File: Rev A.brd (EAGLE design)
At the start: 160 x 100 mm, 21 parts

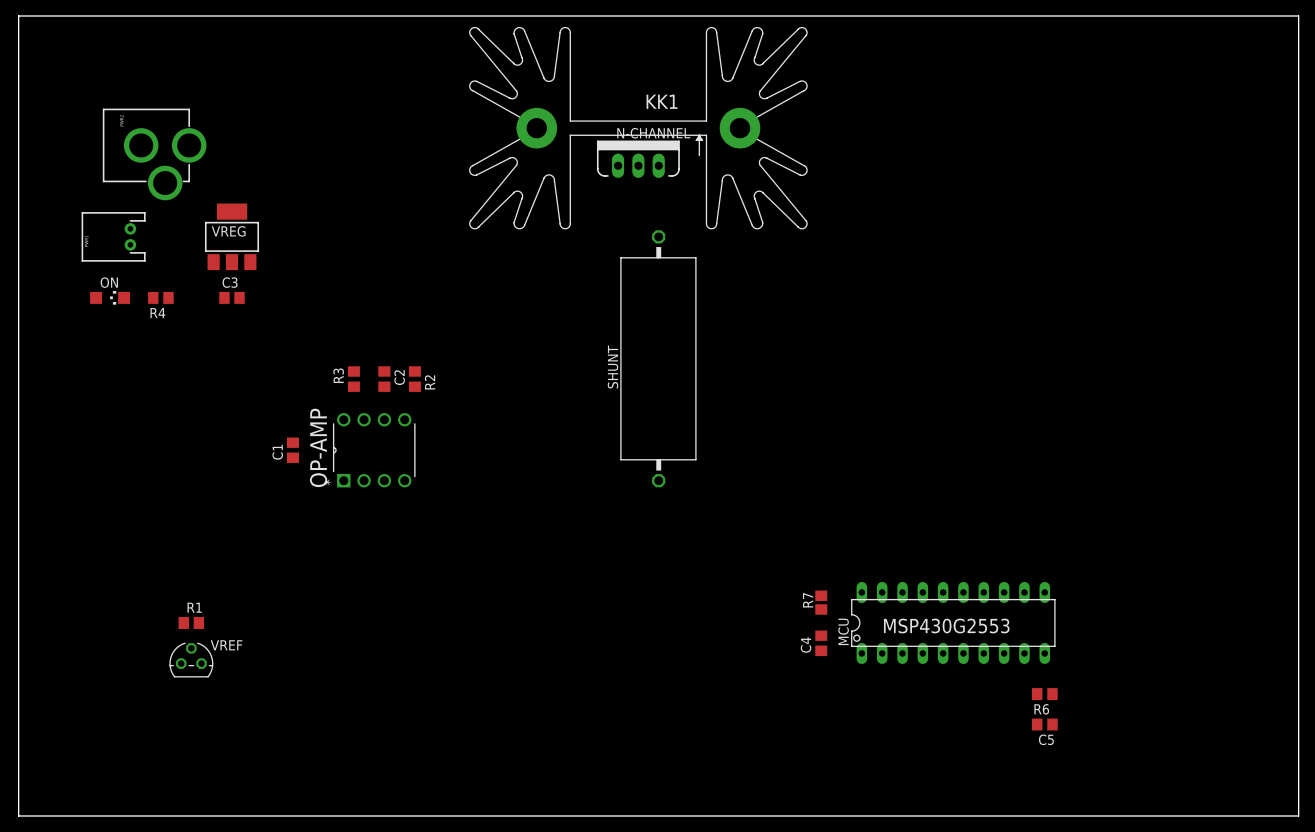
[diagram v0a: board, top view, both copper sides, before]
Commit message: Started working on some blocks on the PCB design
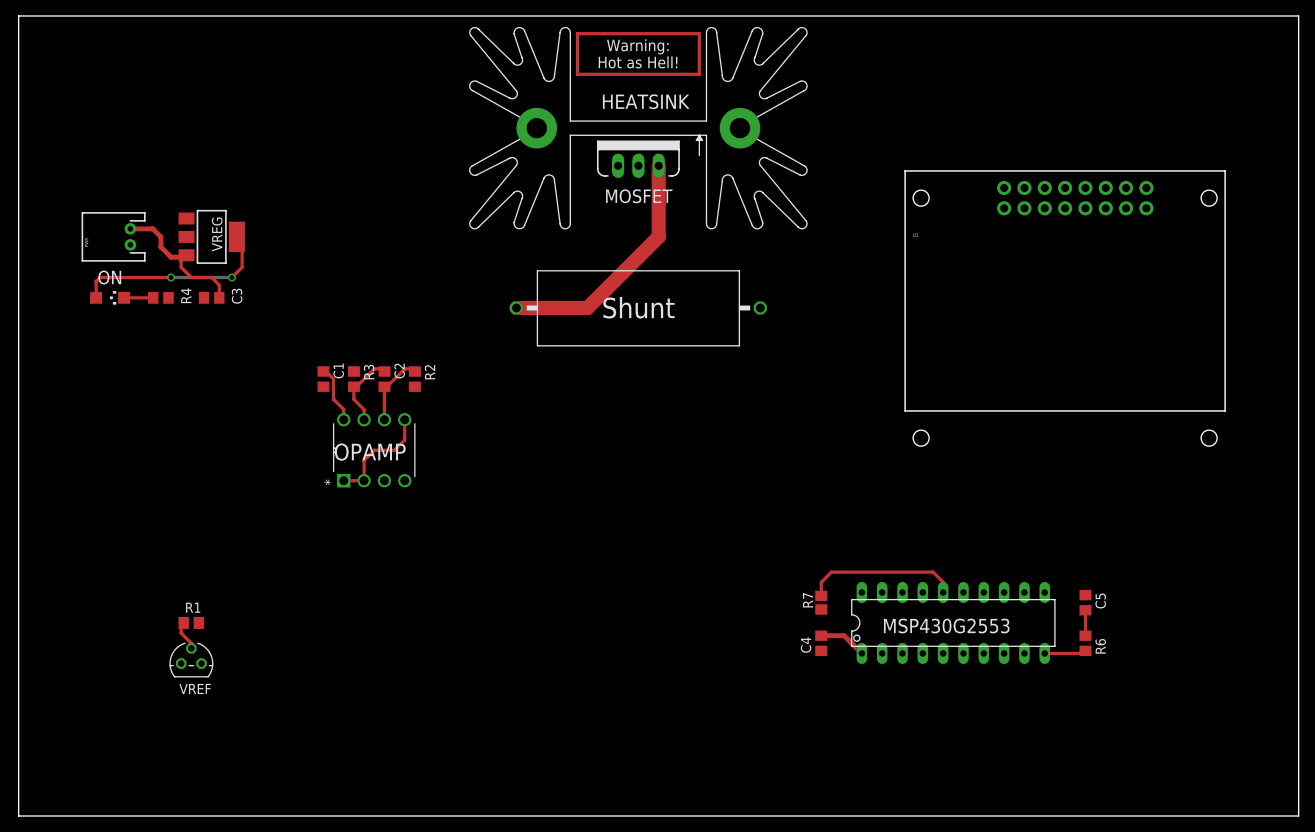
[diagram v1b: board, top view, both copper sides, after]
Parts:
- removed PWR2: POWER_JACKPTH, SparkFun-Connectors:POWER_JACK_PTH
- added U1: LCD-16X28X2, SparkFun-Displays:LCD-8X2
- moved C5 16.1 mm to (133.3, 26.7), turned to 270 degrees
- moved C1 9.67 mm to (38.1, 54.6)
- moved R6 8.13 mm to (133.3, 21.6), turned to 270 degrees
- moved SHUNT 6.84 mm to (77.5, 63.5), turned to 180 degrees
- moved C3 2.54 mm to (24.1, 64.8)
- moved VREG 2.54 mm to (24.1, 72.4), turned to 270 degrees
- renumbered KK1 to HEATSINK, OP-AMP to OPAMP, PWR1 to PWR
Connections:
- net GND: now also U1.1, U1.16; no longer PWR2.GND, PWR2.GNDBREAK
- net N$6: no longer PWR2.PWR
- net VCC: now also U1.15, U1.2
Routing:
- net N$5: track 0.00 -> 40.6 mm
- net VCC: track 0.00 -> 32.9 mm, vias 0 -> 2
- net N$1: track 0.00 -> 30.4 mm
- net N$9: track 0.00 -> 19.3 mm
- net N$6: track 0.00 -> 18.4 mm
- net CURR_SET: track 0.00 -> 13.8 mm
- net REF_SUPPLY: track 0.00 -> 9.83 mm
- net N$4: track 0.00 -> 9.52 mm
- net N$2: track 0.00 -> 8.99 mm
- net N$8: track 0.00 -> 5.22 mm
- net N$7: track 0.00 -> 3.65 mm
- net PWM_FILTERED: track 0.00 -> 3.18 mm
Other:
- board text added: "MOSFET"
- board text added: "ON"
- board text added: "Shunt"
- board text added: "Warning: Hot as Hell!"

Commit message: Removed the voltage reference
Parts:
- removed R1: 2.2kΩ, rcl:R0805
- removed VREF: LM336LP, linear:TO92
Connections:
- removed net REF_SUPPLY: C4.2, MCU.1, R1.1, R7.1, VREF.2
- net GND: no longer VREF.3
- net VCC: now also C4.2, MCU.1, R7.1; no longer R1.2
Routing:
- net REF_SUPPLY: track 9.83 -> 0.00 mm
- net VCC: track 32.9 -> 42.1 mm
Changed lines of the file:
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@@
 <attribute name="VALUE" x="22.86" y="62.23" size="1.27" layer="27"/>
-</element>
-<element name="VREF" library="linear" package="TO92" value="LM336LP" x="21.59" y="19.05" smashed="yes">
-<attribute name="NAME" x="24.13" y="16.51" size="1.27" layer="25" ratio="10" rot="R180"/>
-<attribute name="VALUE" x="24.511" y="17.78" size="1.27" layer="27" ratio="10"/>
-</element>
-<element name="R1" library="rcl" package="R0805" value="2.2kΩ" x="21.59" y="24.13" smashed="yes">
-<attribute name="NAME" x="22.86" y="26.67" size="1.27" layer="25" rot="R180"/>
-<attribute name="VALUE" x="20.955" y="21.59" size="1.27" layer="27"/>
 </element>
 <element name="ON" library="led" package="CHIPLED_1206" value="" x="11.43" y="64.77" smashed="yes" rot="R270">
@@
 <contactref element="VREG" pad="1"/>
 <contactref element="C3" pad="1"/>
-<contactref element="VREF" pad="3"/>
 <contactref element="R4" pad="1"/>
 <contactref element="MCU" pad="20"/>
@@
 <wire x1="13.97" y1="71.39" x2="18.73" y2="64.77" width="0" layer="19" extent="1-1"/>
 <wire x1="20.98" y1="74.69" x2="13.97" y2="71.39" width="0" layer="19" extent="1-1"/>
-<wire x1="22.86" y1="19.05" x2="48.26" y2="41.91" width="0" layer="19" extent="1-1"/>
 </signal>
 <signal name="VCC">
@@
 <contactref element="C1" pad="2"/>
 <contactref element="VREG" pad="4"/>
-<contactref element="R1" pad="2"/>
 <contactref element="ON" pad="A"/>
 <wire x1="40.64" y1="49.53" x2="40.64" y2="50.8" width="0.4064" layer="1"/>
@@
 <contactref element="U1" pad="2"/>
 <contactref element="U1" pad="15"/>
+<contactref element="MCU" pad="1"/>
+<contactref element="C4" pad="2"/>
+<wire x1="100.33" y1="22.54" x2="103.19" y2="22.54" width="0.4064" layer="1"/>
+<wire x1="103.19" y1="22.54" x2="104.14" y2="21.59" width="0.4064" layer="1"/>
+<wire x1="104.14" y1="21.59" x2="104.14" y2="21.585" width="0.4064" layer="1"/>
+<wire x1="104.14" y1="21.585" x2="105.405" y2="20.32" width="0.4064" layer="1"/>
+<contactref element="R7" pad="1"/>
 <wire x1="123.19" y1="78.5" x2="140.97" y2="75.96" width="0" layer="19" extent="1-1"/>
-<wire x1="40.64" y1="50.8" x2="123.19" y2="78.5" width="0" layer="19" extent="1-1"/>
+<wire x1="100.33" y1="25.82" x2="123.19" y2="78.5" width="0" layer="19" extent="1-1"/>
+<wire x1="40.64" y1="49.53" x2="100.33" y2="25.82" width="0" layer="19" extent="1-1"/>
 <wire x1="26.67" y1="67.31" x2="38.1" y2="55.88" width="0" layer="19" extent="1-1"/>
-<wire x1="22.54" y1="24.13" x2="40.64" y2="49.53" width="0" layer="19" extent="1-1"/>
+<wire x1="100.33" y1="25.82" x2="100.33" y2="22.54" width="0.4064" layer="1"/>
 </signal>
 <signal name="N$2">
@@
 <wire x1="20.74" y1="69.85" x2="20.98" y2="70.09" width="0.6096" layer="1"/>
 </signal>
-<signal name="REF_SUPPLY">
-<contactref element="VREF" pad="2"/>
-<contactref element="R1" pad="1"/>
-<contactref element="MCU" pad="1"/>
-<contactref element="C4" pad="2"/>
-<contactref element="R7" pad="1"/>
-<wire x1="21.59" y1="20.955" x2="21.59" y2="21.59" width="0.4064" layer="1"/>
-<wire x1="21.59" y1="21.59" x2="20.32" y2="22.86" width="0.4064" layer="1"/>
-<wire x1="20.32" y1="22.86" x2="20.32" y2="23.81" width="0.4064" layer="1"/>
-<wire x1="20.32" y1="23.81" x2="20.64" y2="24.13" width="0.4064" layer="1"/>
-<wire x1="100.33" y1="25.82" x2="100.33" y2="22.54" width="0" layer="19" extent="1-1"/>
-<wire x1="21.59" y1="20.955" x2="100.33" y2="22.54" width="0" layer="19" extent="1-1"/>
-<wire x1="100.33" y1="22.54" x2="103.19" y2="22.54" width="0.6096" layer="1"/>
-<wire x1="103.19" y1="22.54" x2="104.14" y2="21.59" width="0.6096" layer="1"/>
-<wire x1="104.14" y1="21.59" x2="104.14" y2="21.585" width="0.6096" layer="1"/>
-<wire x1="104.14" y1="21.585" x2="105.405" y2="20.32" width="0.6096" layer="1"/>
-</signal>
 <signal name="N$7">

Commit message: Did a lot of stuff
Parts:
- removed OPAMP: TLV2372IP, Texas Instruments_By_element14_Batch_1:DIP254P762X508-8
- added 5VREG: 78L05SMD, linear:SO08
- added C6, C9: 0.1uF, rcl:C0805
- added C7: 10uF, rcl:E2,5-6
- added JP_BKL: (no value), pinhead:2X02
- added OP1, OP2: TLV2372IP, Texas Instruments_By_element14_Batch_1:DIP254P762X508-8
- added R8: 10kΩ, rcl:R0805
- added RE1: ROTARTY_ENCODER, SparkFun-Electromechanical:ROTARY_ENC_PLAIN
- added VO: 10kΩ, bourns:3386G
- moved C4 91.2 mm to (12.7, 47.0)
- moved C5 91.2 mm to (45.7, 52.1)
- moved MCU 91.2 mm to (29.2, 49.5)
- moved R6 91.2 mm to (45.7, 47.0)
- moved R7 91.2 mm to (12.7, 52.1)
- moved C2 26.9 mm to (71.1, 45.7)
- moved R2 26.9 mm to (74.9, 45.7)
- moved R3 26.9 mm to (67.3, 45.7)
- moved C1 26.9 mm to (63.5, 45.7)
- renumbered U1 to LCD, VREG to 3VREG
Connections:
- removed net N$2: C2.2, OPAMP.6, R2.1
- new net +5V: 5VREG.1, C9.2, JP_BKL.4, LCD.2, VO.1
- new net CURR_SENSE: MCU.14, OP2.1, OP2.2
- new net DB4: LCD.11, MCU.11
- new net DB5: LCD.12, MCU.12
- new net DB6: LCD.13, MCU.13
- new net DB7: LCD.14, MCU.6
- new net LCD_EN: LCD.6, MCU.9
- new net N$1: C2.2, OP1.6, OP2.3, R2.1
- new net N$10: LCD.3, VO.2
- new net N$11: JP_BKL.3, LCD.15
- new net RE_A: MCU.7, RE1.A
- new net RE_B: MCU.15, RE1.B
- new net RE_BTN: MCU.5, R8.1, RE1.SW-
- new net RS: LCD.4, MCU.8
- net CURR_SET: now also OP1.1, OP1.2, OP1.5; no longer OPAMP.1, OPAMP.2, OPAMP.5
- net GND: now also 5VREG.2, 5VREG.3, 5VREG.6, 5VREG.7, C6.1, C7.-, C9.1, LCD.5, OP1.4, OP2.4, RE1.C, RE1.SW+, VO.3; no longer OPAMP.4
- net N$4: now also OP1.7; no longer OPAMP.7
- net N$6: now also 5VREG.8
- net PWM_FILTERED: now also OP1.3; no longer OPAMP.3
- net VCC: now also C6.2, C7.+, OP1.8, OP2.8, R8.2; no longer LCD.15, LCD.2, OPAMP.8
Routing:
- net N$1: track 0.00 -> 31.2 mm
- net VCC: track 42.1 -> 72.6 mm
- net N$6: track 18.4 -> 39.2 mm
- net +5V: track 0.00 -> 13.7 mm
- net N$2: track 8.99 -> 0.00 mm
- net RE_BTN: track 0.00 -> 5.10 mm
- net CURR_SENSE: track 0.00 -> 2.54 mm
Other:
- board text added: "Backlight"
- board text added: "Contrast"
- board text added: "OFF"

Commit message: Looks good to me
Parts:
- added 3V3, 5V, GND, IV, IVO, SGND: PTR1TP10SQ, testpad:TP10SQ
- added PWR_IN: M02JST-PTH-2, SparkFun-Connectors:JST-2-PTH
- added U$1: (no value), dicons:ICON_TEMP
- added U$2: (no value), dicons:ICON_EXL-S
- added U$3: (no value), dicons:ICON_BATTERY-S
- moved VO 118.6 mm to (16.5, 30.5)
- moved LCD 106.1 mm to (26.7, 41.9)
- moved JP_BKL 78.8 mm to (53.3, 27.9)
- moved HEATSINK 39.5 mm to (74.9, 45.7)
- moved N-CHANNEL 39.5 mm to (74.9, 41.9)
- moved SHUNT 39.5 mm to (74.9, 24.1)
- moved C6 36.1 mm to (80.0, 10.2), turned to 90 degrees
- moved C4 33.1 mm to (10.2, 14.0)
- moved R6 33.1 mm to (43.2, 14.0)
- moved C5 33.1 mm to (43.2, 19.1)
- moved MCU 33.1 mm to (26.7, 16.5)
- moved R7 33.1 mm to (10.2, 19.1)
- moved R2 30.7 mm to (59.7, 19.1)
- moved OP1 30.7 mm to (58.4, 14.0)
- moved OP2 30.7 mm to (74.9, 14.0)
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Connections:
- net +5V: now also 5V.TP
- net CURR_SENSE: now also IVO.TP
- net GND: now also GND.TP, PWR_IN.1, SGND.TP
- net N$13: now also IV.TP
- net TVIN: now also PWR_IN.2
- net VCC: now also 3V3.TP
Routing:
- net VCC: track 72.6 -> 195.5 mm, vias 2 -> 9
- net +5V: track 13.7 -> 104.1 mm, vias 0 -> 5
- net RE_B: track 0.00 -> 83.8 mm
- net RE_BTN: track 5.10 -> 87.7 mm, vias 0 -> 2
- net LCD_EN: track 0.00 -> 76.5 mm, vias 0 -> 4
- net RS: track 0.00 -> 65.9 mm, vias 0 -> 3
- net RE_A: track 0.00 -> 65.6 mm
- net DB7: track 0.00 -> 63.8 mm
- net CURR_SENSE: track 2.54 -> 47.7 mm, vias 0 -> 2
- net N$11: track 0.00 -> 43.9 mm, vias 0 -> 1
- net DB5: track 0.00 -> 40.6 mm, vias 0 -> 1
- net DB6: track 0.00 -> 40.5 mm
- net TVIN: track 0.00 -> 40.3 mm
- net DB4: track 0.00 -> 38.0 mm, vias 0 -> 1
- net N$3: track 0.00 -> 34.8 mm
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- added copper zone on layer 1, net GND
- added copper zone on layer 16, net GND
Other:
- board size 160 x 100 mm -> 100.3 x 61 mm
- board text added: "Electronic DC Load"
- board text added: "Input"
- board text added: "Nathan Campos, 2013"
- board text added: "miniLoad"
